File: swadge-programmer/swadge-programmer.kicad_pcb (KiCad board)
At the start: 2 copper layers, 73.7 x 73.7 mm, 27 parts, among them J1 USB_B_Micro, J2 Conn_02x15_Top_Bottom, J3 Conn_02x15_Top_Bottom, J4 ftdi-header, J5 Conn_01x03_Male, SW1 4-1437565-2, SW2 4-1437565-2, SW3 4-1437565-2, SW4 SW_DPDT_x2, SW5 SW_DPDT_x2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

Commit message: Cleanup text and tracks
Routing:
- net Net-(R5-Pad1): track 44.4 -> 45.1 mm
- net +3V3: track 91.0 -> 91.5 mm
- net +5V: track 62.0 -> 61.6 mm, vias 1 -> 2
- net GND: track 12.7 -> 12.8 mm, vias 18 -> 19
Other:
- board text added: "1 2 3 4 5 6 7 8 9 0 11 12 13 14 15"
- board text added: "GND CTS VCC TXD RXD RTS"
- board text removed: "(G0)SCL"
- board text removed: "(G12)SW3"
- board text removed: "(G13)SW2"
- board text removed: "(G14)AUD_PWR"
- board text removed: "(G15)_RES"
- board text removed: "(G16)REST"
- board text removed: "(G2)SDA"
- board text removed: "(G4)SW4"
- board text removed: "(G5)SW5"
- board text removed: "(TOUT)ADC_PIN"
- board text removed: "GND"
- board text removed: "RX"
- board text removed: "TX"

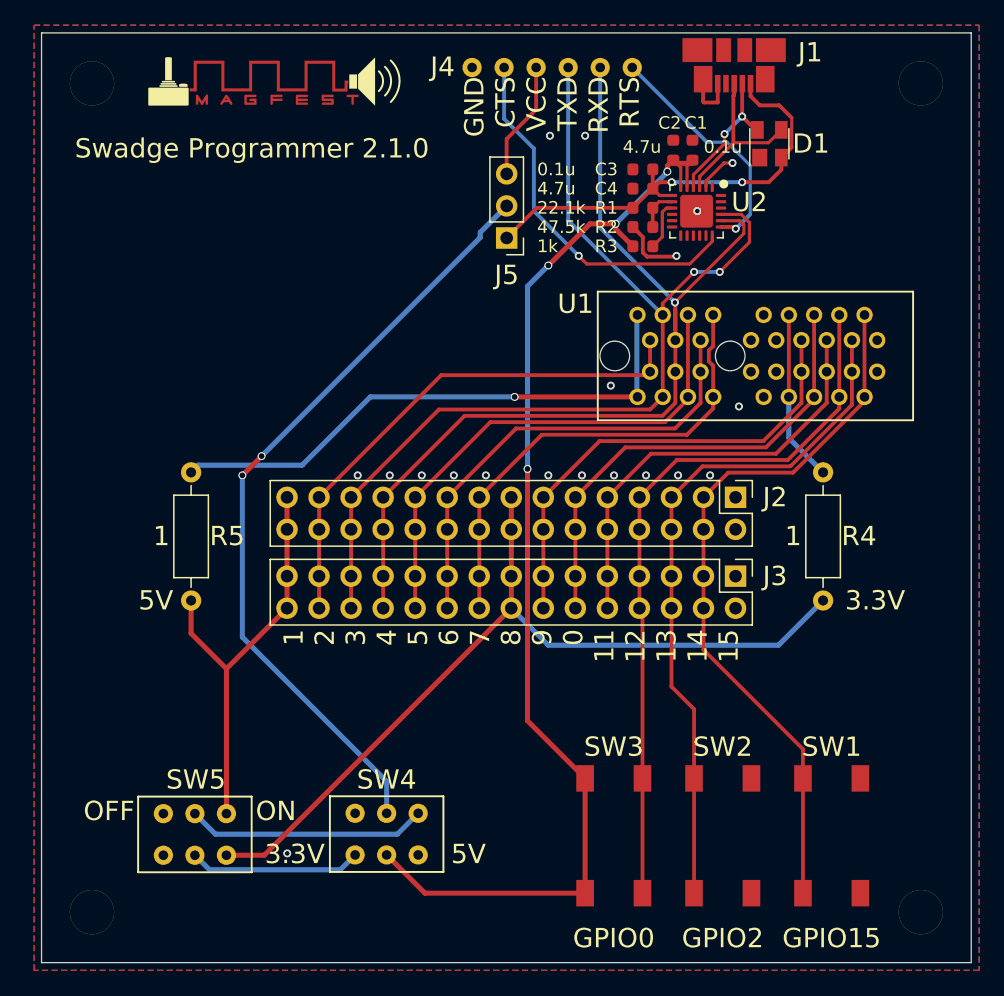
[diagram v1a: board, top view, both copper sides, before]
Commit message: Round corners, clean up text
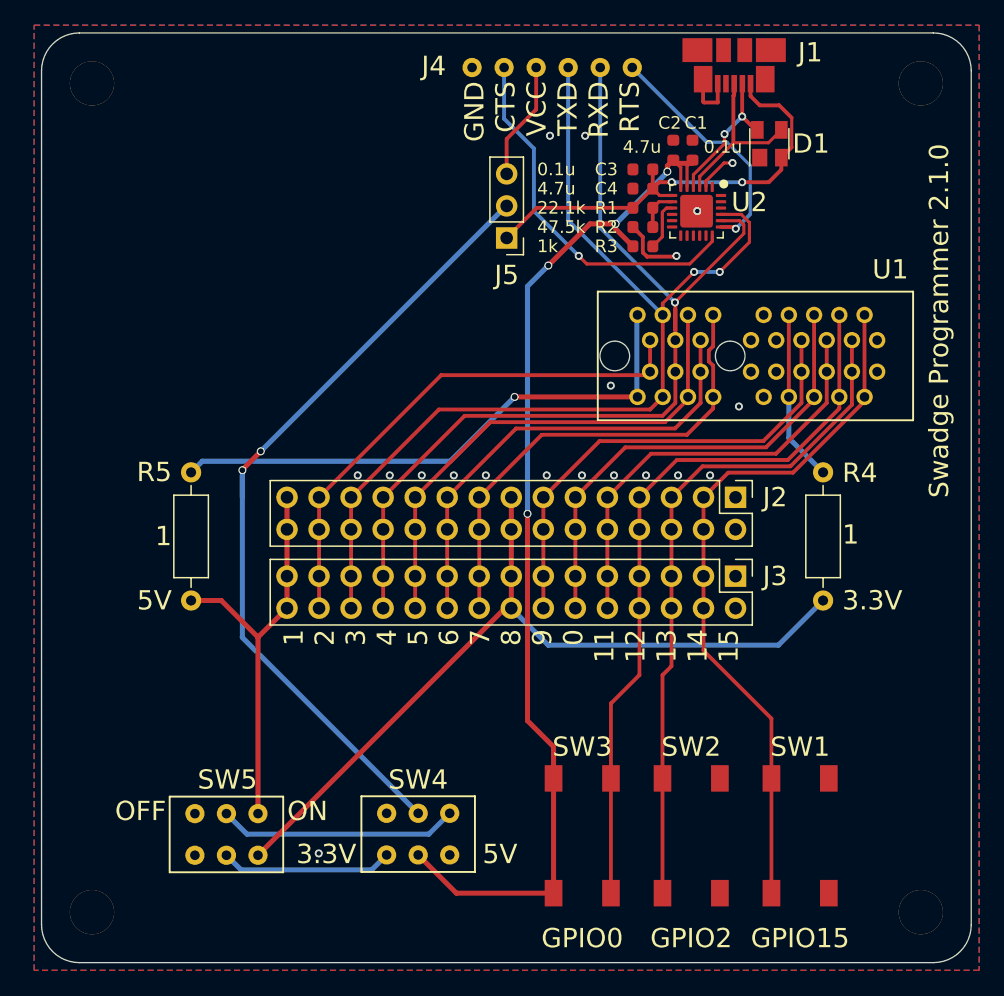
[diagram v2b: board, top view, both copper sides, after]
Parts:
- removed svg2mod: G***, Swadge_Parts:MAGFEST_logo_centered_final
- moved SW1 2.50 mm to (168.7, 113.8)
- moved SW2 2.50 mm to (160.0, 113.8)
- moved SW3 2.50 mm to (151.4, 113.8)
- moved SW4 2.50 mm to (138.4, 113.7)
- moved SW5 2.50 mm to (123.2, 113.7)
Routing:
- net +3V3: track 91.5 -> 85.5 mm
- net +5V: track 61.6 -> 64.3 mm
- net 3.3V: track 66.9 -> 64.4 mm
- net 5V: track 33.6 -> 32.5 mm
- net SCL: track 57.4 -> 56.4 mm
- net _RES: track 57.7 -> 58.5 mm
- net Net-(R5-Pad1): track 45.1 -> 44.4 mm
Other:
- outline, holes or cut-outs redrawn

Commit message: Update text
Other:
- board text added: "+5V SW4 RX TX SW5 REST ADC +3.3V SW1 SW3 SW2 _RES SDA SCL GND"
- board text removed: "1 2 3 4 5 6 7 8 9 0 11 12 13 14 15"

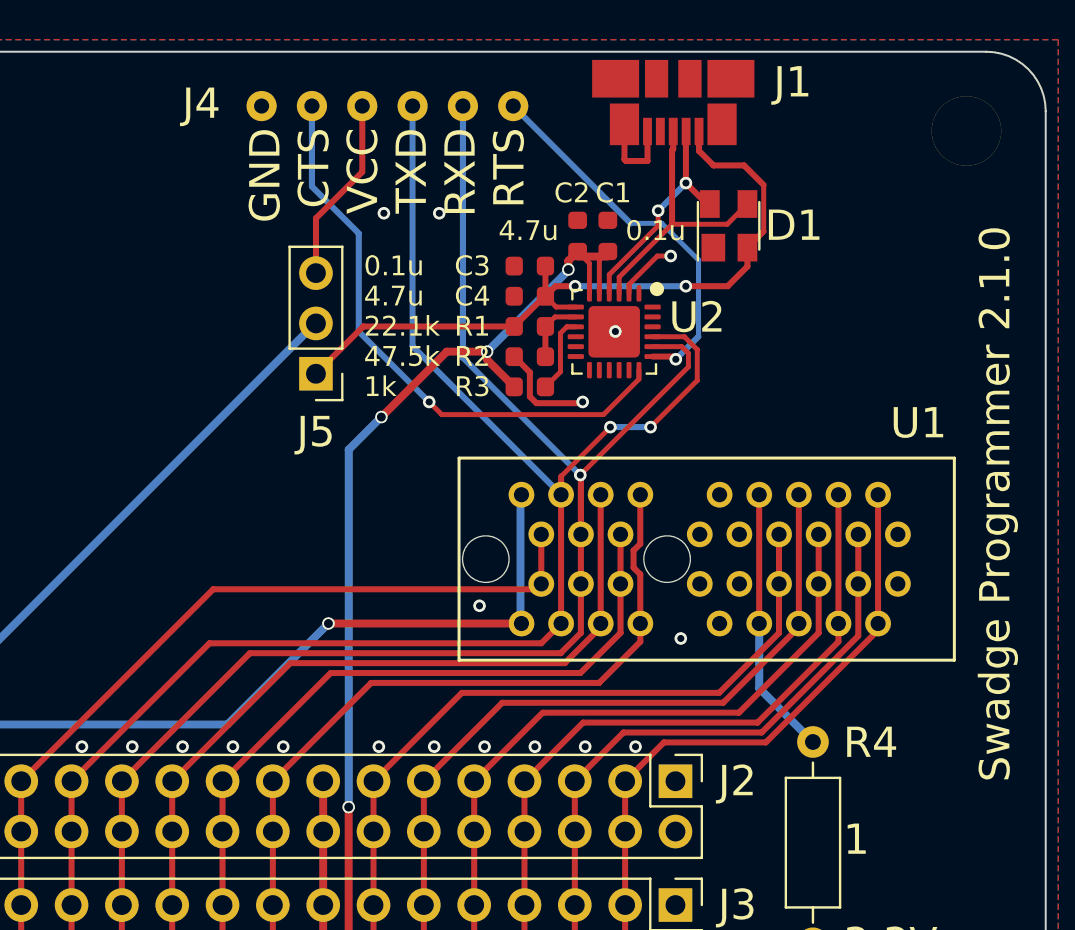
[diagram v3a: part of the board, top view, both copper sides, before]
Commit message: Adjusted PCIe position
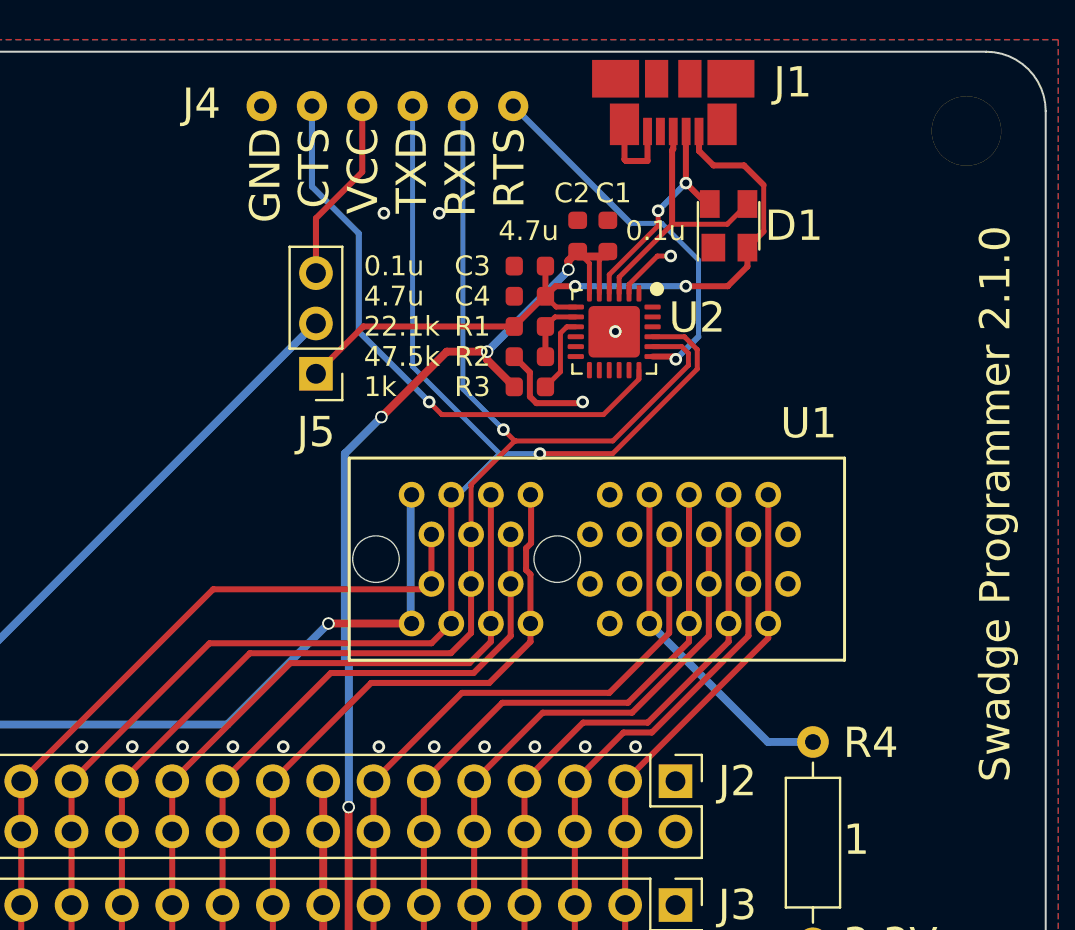
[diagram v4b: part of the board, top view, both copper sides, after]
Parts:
- moved U1 5.54 mm to (157.6, 75.8)
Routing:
- net ADC_PIN: track 38.0 -> 32.3 mm
- net Net-(R5-Pad1): track 44.4 -> 38.9 mm
- net SW4: track 41.7 -> 36.1 mm
- net SDA: track 54.1 -> 48.6 mm
- net _RES: track 58.5 -> 53.0 mm
- net AUD_PWR: track 37.3 -> 31.8 mm
- net REST: track 37.0 -> 31.5 mm
- net SW2: track 34.3 -> 28.8 mm
- net SCL: track 56.4 -> 51.1 mm
- net SW5: track 40.3 -> 35.2 mm
- net SW3: track 37.6 -> 32.5 mm
- net TX: track 76.1 -> 71.0 mm
- net RX: track 80.3 -> 75.7 mm, vias 2 -> 1
- net Net-(R4-Pad1): track 13.6 -> 17.2 mm
- net GND: vias 19 -> 17

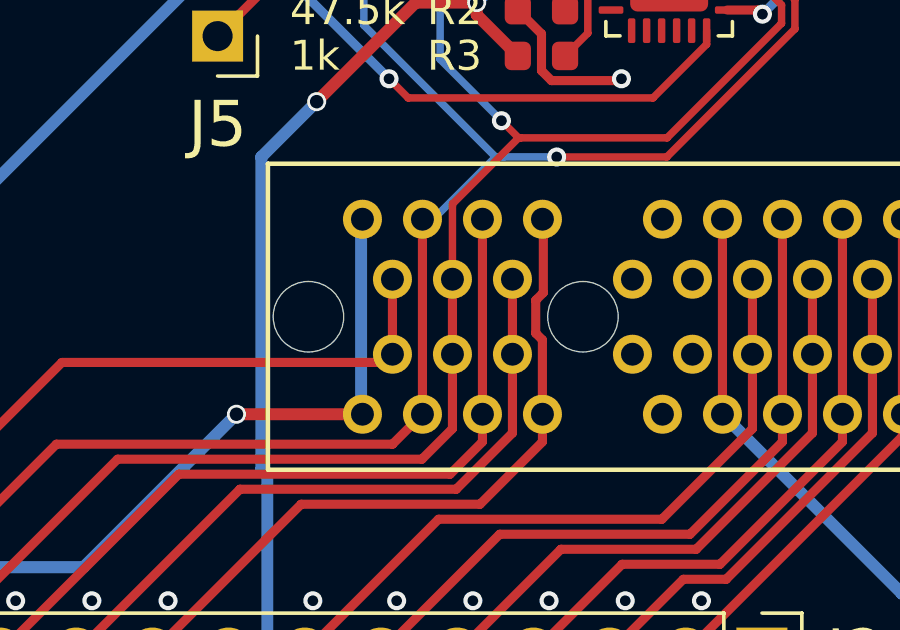
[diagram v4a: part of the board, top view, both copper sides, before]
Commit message: Added missing vias
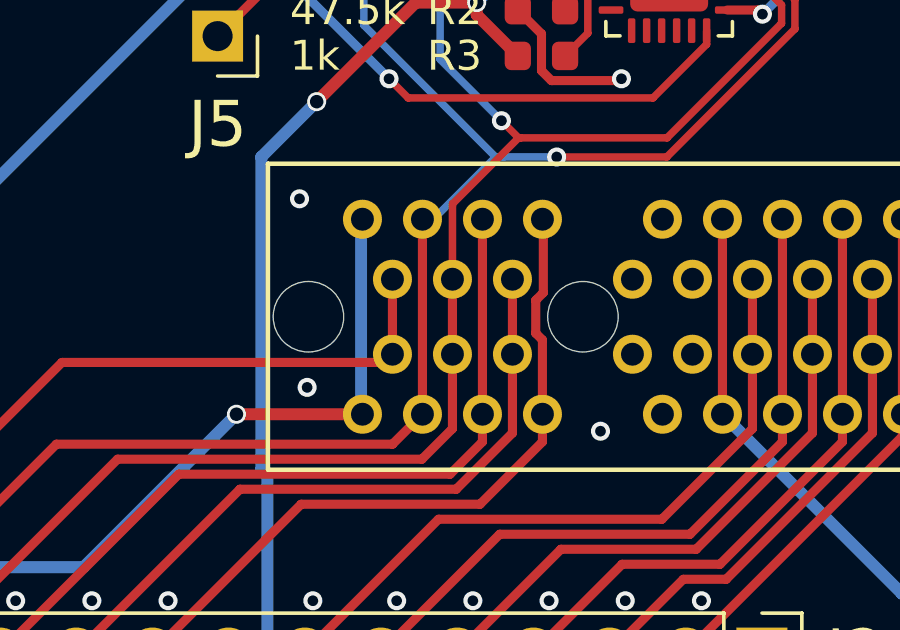
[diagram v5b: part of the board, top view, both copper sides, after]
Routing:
- net GND: vias 17 -> 20

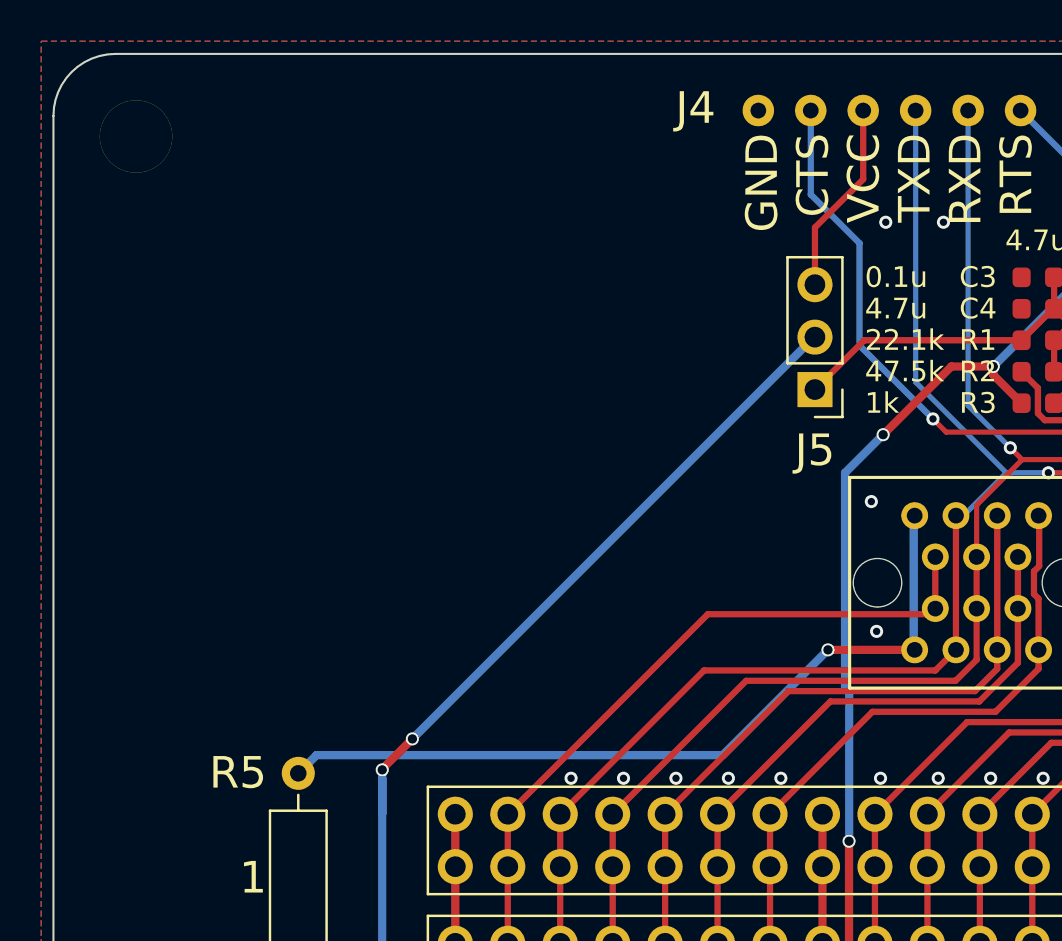
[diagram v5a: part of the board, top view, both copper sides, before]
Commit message: Added graphic to programmer
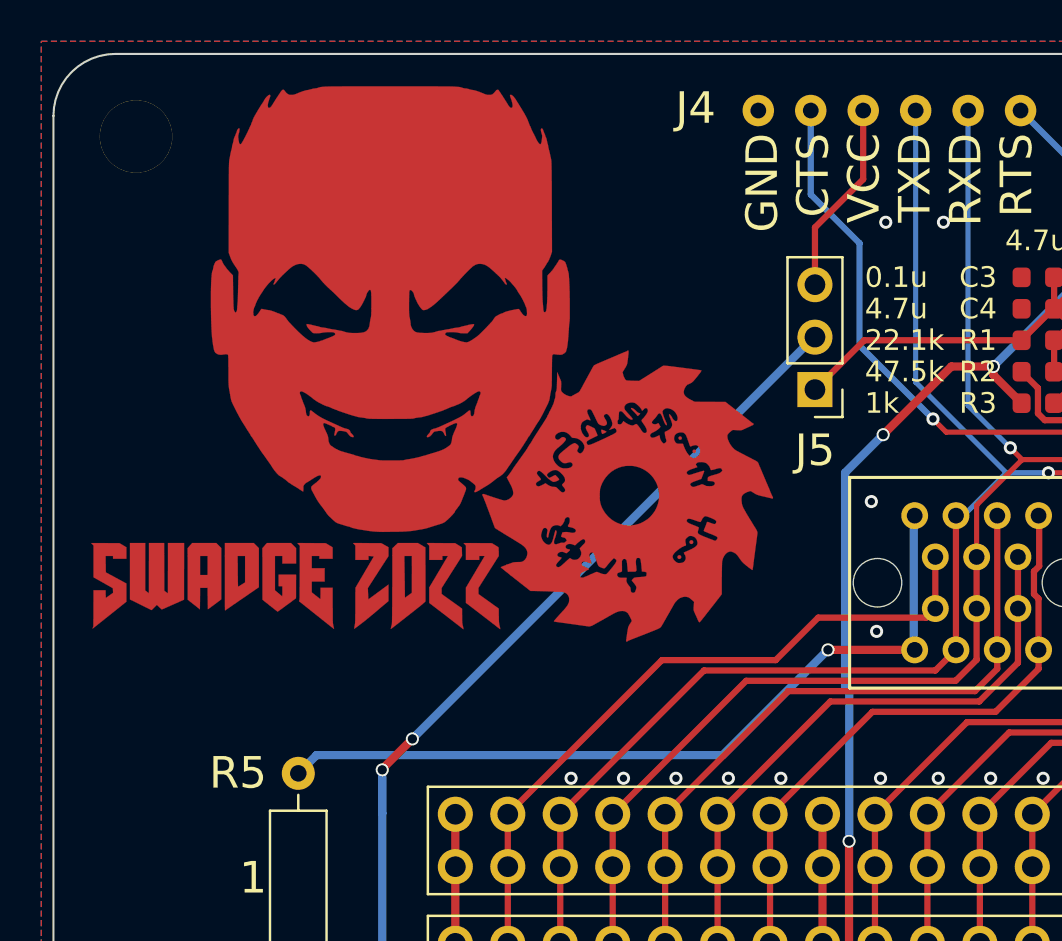
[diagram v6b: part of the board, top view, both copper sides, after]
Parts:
- added Ref**: Val**, swadge-programmer:programmer-graphic, F.Cu at (126.9, 65.2)

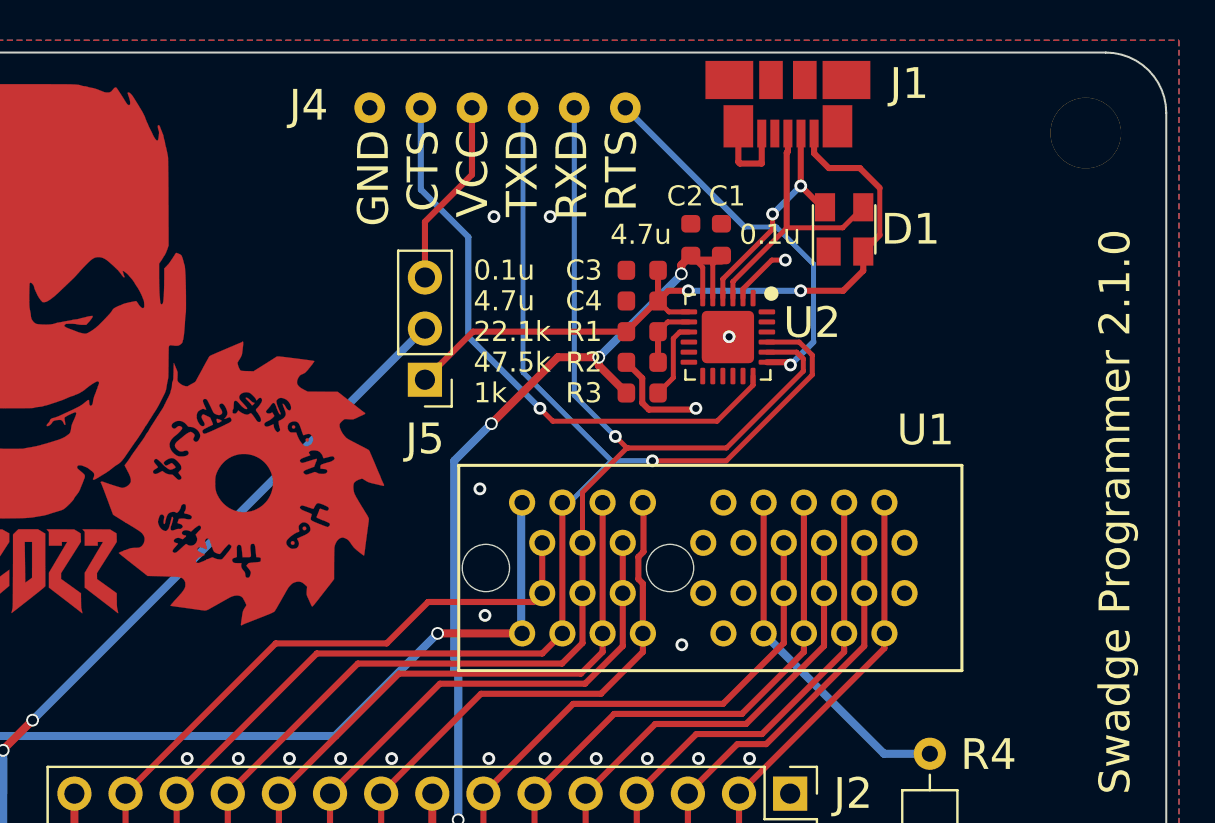
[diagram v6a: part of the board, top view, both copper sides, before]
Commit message: Added pin for LED OUT
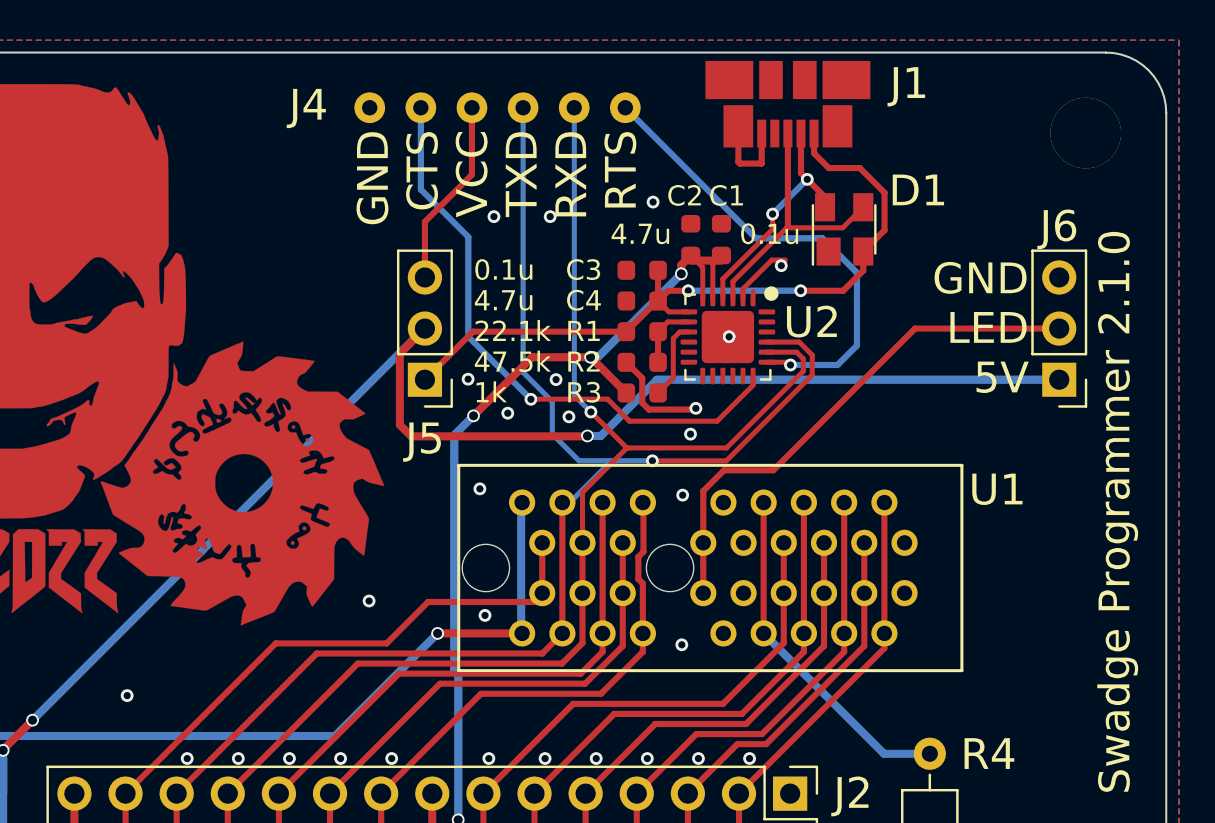
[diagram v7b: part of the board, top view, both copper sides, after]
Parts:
- added J6: Conn_01x03_Male, Swadge_Parts:PinHeader_1x03_P2.54mm_Vertical, F.Cu at (176.9, 66.4)
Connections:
- J1 pad 4: (no net) -> Net-(J1-Pad4)
- SW4 pad 3: (no net) -> Net-(SW4-Pad3)
- SW4 pad 4: (no net) -> Net-(SW4-Pad4)
- SW5 pad 3: (no net) -> Net-(SW5-Pad3)
- SW5 pad 6: (no net) -> Net-(SW5-Pad6)
- U1 pad A10: (no net) -> Net-(U1-PadA10)
- U1 pad A11: (no net) -> LED_OUT
- U1 pad A9: (no net) -> Net-(U1-PadA9)
- U1 pad B10: (no net) -> Net-(U1-PadB10)
- U1 pad B11: (no net) -> LED_OUT
- U1 pad B9: (no net) -> Net-(U1-PadB9)
- U2 pad 1: (no net) -> Net-(U2-Pad1)
- U2 pad 10: (no net) -> Net-(U2-Pad10)
- U2 pad 11: (no net) -> Net-(U2-Pad11)
- U2 pad 12: (no net) -> Net-(U2-Pad12)
- U2 pad 13: (no net) -> Net-(U2-Pad13)
- U2 pad 14: (no net) -> Net-(U2-Pad14)
- U2 pad 15: (no net) -> Net-(U2-Pad15)
- U2 pad 16: (no net) -> Net-(U2-Pad16)
- U2 pad 17: (no net) -> Net-(U2-Pad17)
- U2 pad 22: (no net) -> Net-(U2-Pad22)
- U2 pad 23: (no net) -> Net-(U2-Pad23)
- U2 pad 24: (no net) -> Net-(U2-Pad24)
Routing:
- net +5V: track 64.3 -> 103.8 mm, vias 2 -> 3
- net LED_OUT: track 0.00 -> 26.1 mm
- net CTS: track 19.3 -> 23.5 mm
- net RX: track 75.7 -> 76.6 mm
- net +3V3: track 85.6 -> 86.6 mm
- net Net-(D1-Pad4): track 11.4 -> 12.0 mm
- net GND: vias 20 -> 29
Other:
- board text added: "GND LED 5V"
